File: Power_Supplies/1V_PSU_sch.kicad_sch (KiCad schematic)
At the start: 9 parts, among them U7 TPS62822DLC

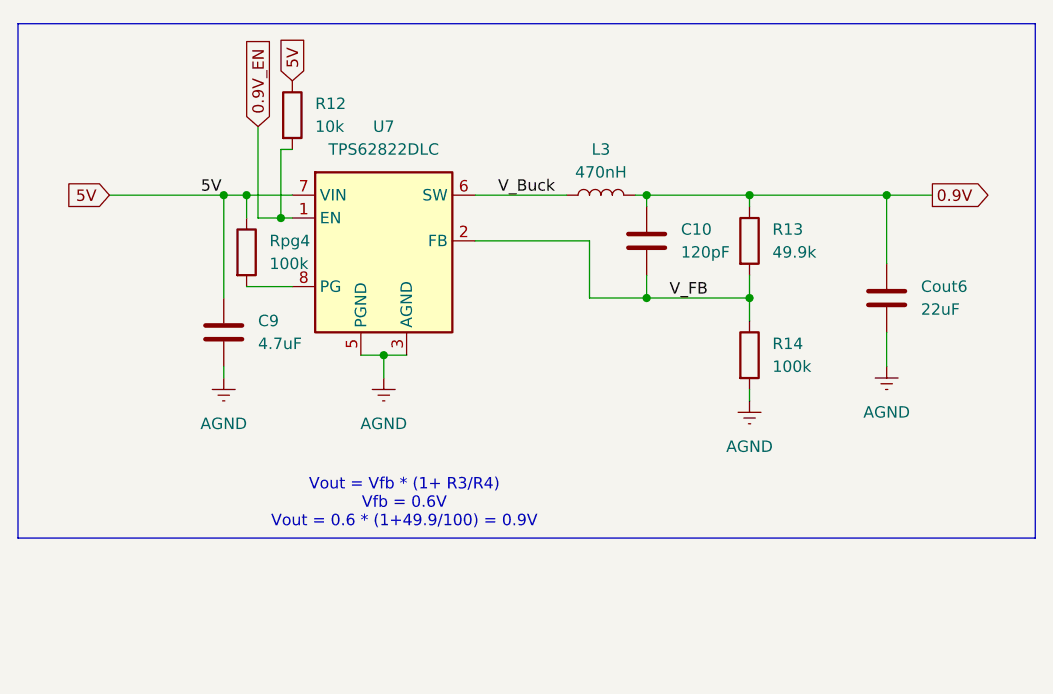
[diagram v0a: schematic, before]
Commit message: Added stuff for the power supply circuitry
changed all grounds to GND (same ground plane)
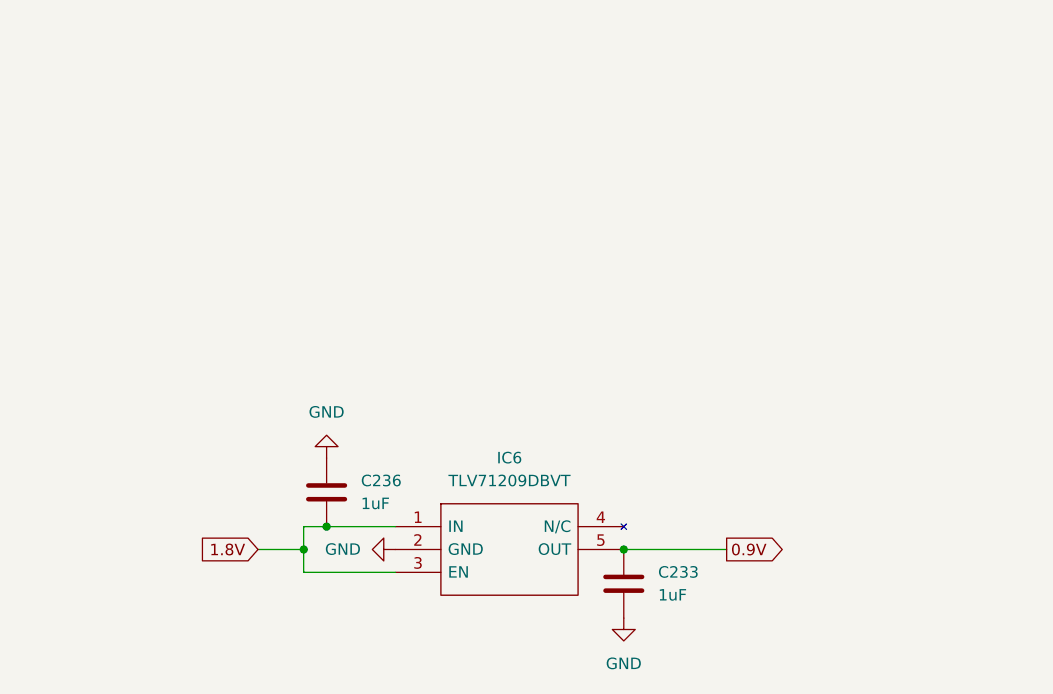
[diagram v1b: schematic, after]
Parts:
- removed C10: 120pF, Capacitor_SMD:C_0402_1005Metric, symbol Device:C
- removed C9: 4.7uF, Capacitor_SMD:C_0805_2012Metric, symbol Device:C
- removed Cout6: 22uF, Capacitor_SMD:C_0805_2012Metric, symbol Device:C
- removed L3: 470nH, Inductor_SMD:L_0805_2012Metric, symbol Device:L
- removed R12: 10k, PCM_Resistor_SMD_AKL:R_0805_2012Metric_Pad1.15x1.40mm_HandSolder, symbol Device:R
- removed R13: 49.9k, PCM_Resistor_SMD_AKL:R_0805_2012Metric_Pad1.15x1.40mm_HandSolder, symbol Device:R
- removed R14, Rpg4: 100k, PCM_Resistor_SMD_AKL:R_0805_2012Metric_Pad1.15x1.40mm_HandSolder, symbol Device:R
- removed U7: TPS62822DLC, Package_SON:Texas_VSON-HR-8_1.5x2mm_P0.5mm, symbol Regulator_Switching:TPS62822DLC
- added C233, C236: 1uF, Capacitor_SMD:C_0402_1005Metric, symbol Device:C
- added IC6: TLV71209DBVT, SOT95P280X145-5N, symbol SamacSys_Parts:TLV71209DBVT
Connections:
- net 0.9V: now also C233.1, IC6.5 (OUT)
- new net 1.8V: C236.2, IC6.1 (IN), IC6.3 (EN)
- new net GND: C233.2, C236.1, IC6.2 (GND)
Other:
- note removed: "Vout = Vfb * (1+ R3/R4) Vfb = 0.6V Vout = 0.6 * (1+49.9/100) = 0.9V"
